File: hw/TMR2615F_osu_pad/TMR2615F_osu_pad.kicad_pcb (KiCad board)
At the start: 4 copper layers, 60 x 60 mm, 120 parts, among them J1 TYPE-C-31-M-12, J10 Conn_01x04, J2 TYPE-C-31-M-12, J3 Conn_01x02, J4 TYPE-C-31-M-12, J5 XY-SH1_0-4A61, J7 Conn_01x10, J8 Conn_01x06, J9 Conn_01x23, SW1 SKSGPAE010, SW2 SKSGPAE010, U1 CA-IS3722CHS, U10 TMR2615x, U11 CPG151101S11-16, U12 SK6812MINI-E, U13 TMR2615x, U14 CPG151101S11-16, U15 SK6812MINI-E, U16 TMR2615x, U17 CPG151101S11-16, U18 SK6812MINI-E, U19 TMR2615x, U2 SRV05-4A, U20 CPG151101S11-16, U21 SK6812MINI-E, U22 TMR2615x, U23 CPG151101S11-16, U24 SK6812MINI-E, U25 TMR2615x, U26 CPG151101S11-16, U27 SK6812MINI-E, U28 SRV05-4A, U3 TMUX1574RSVR, U4 LM66100DCK, U5 AP22653W6-7, U6 SRV05-4A, U7 AT32F405RBT7-7, U8 XC6206P332MR, U9 TPS7A4700, X1 X322512MSB4SI

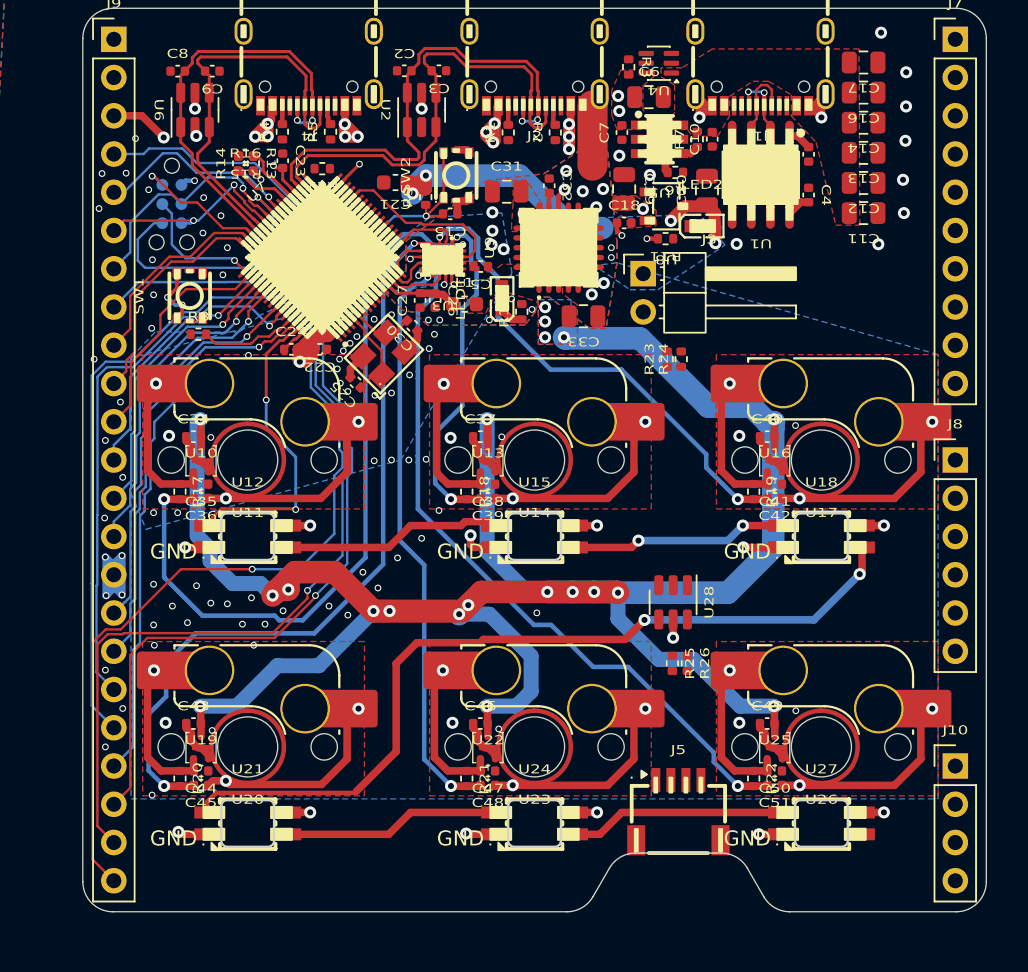
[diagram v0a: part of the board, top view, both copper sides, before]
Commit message: Update TMR2615F_osu_pad layout/schematic, bump library submodule, add ERC report
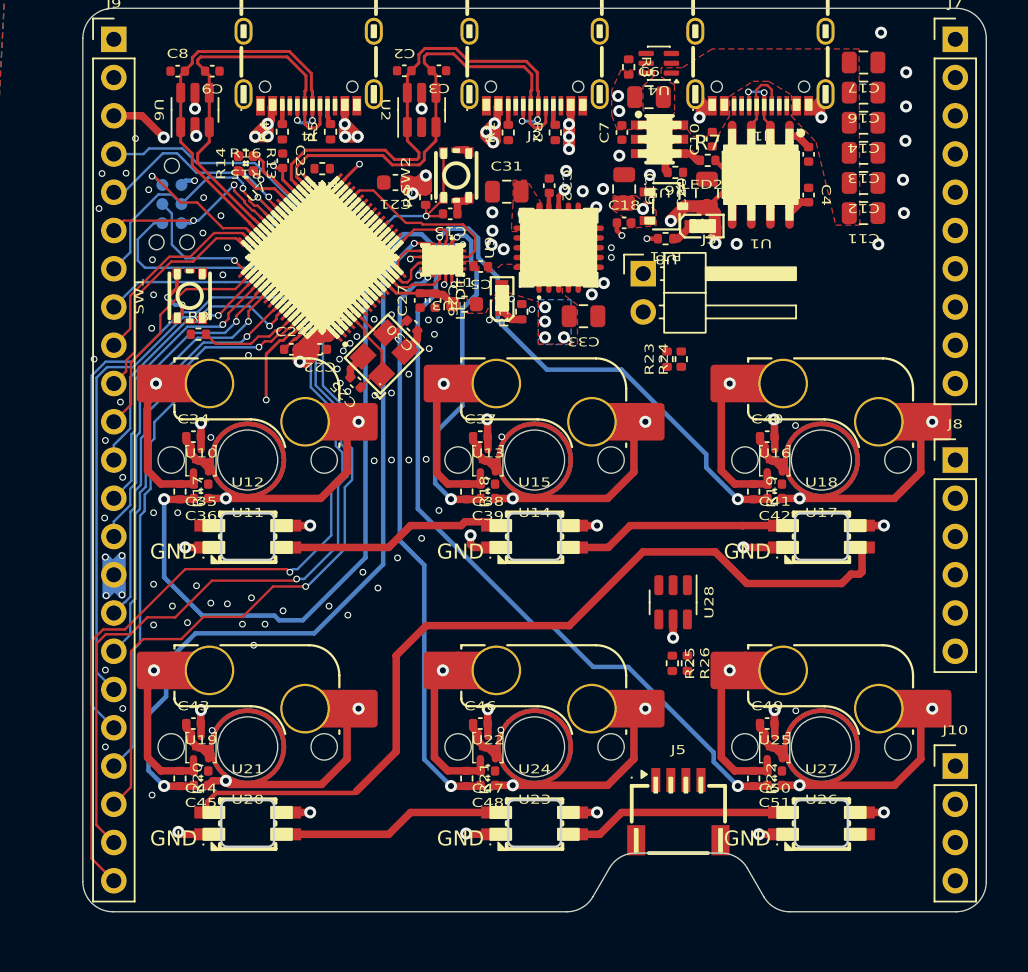
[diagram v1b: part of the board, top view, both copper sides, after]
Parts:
- removed NT1: NetTie_2, NetTie:NetTie-2_SMD_Pad2.0mm
- moved R7 1.57 mm to (124.6, 101.0), turned to 0 degrees
- moved C20 0.20 mm to (124.5, 103.2)
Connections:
- C26 pad 2: GNDA -> GND
- C27 pad 1: GNDA -> GND
- C31 pad 1: GNDA -> GND
- C32 pad 1: GNDA -> GND
- C33 pad 1: GNDA -> GND
- C34 pad 1: GNDA -> GND
- C35 pad 1: GNDA -> GND
- C36 pad 1: GNDA -> GND
- C37 pad 1: GNDA -> GND
- C38 pad 1: GNDA -> GND
- C39 pad 1: GNDA -> GND
- C40 pad 1: GNDA -> GND
- C41 pad 1: GNDA -> GND
- C42 pad 1: GNDA -> GND
- C43 pad 1: GNDA -> GND
- C44 pad 1: GNDA -> GND
- C45 pad 1: GNDA -> GND
- C46 pad 1: GNDA -> GND
- C47 pad 1: GNDA -> GND
- C48 pad 1: GNDA -> GND
- C49 pad 1: GNDA -> GND
- C5 pad 1: GNDA -> GND
- C50 pad 1: GNDA -> GND
- C51 pad 1: GNDA -> GND
- J8 pad 1: GNDA -> GND
- J9 pad 10: /I2C2_SDA -> /I2C2_SCL
- J9 pad 9: /I2C2_SCL -> /I2C2_SDA
- R10 pad 2: GNDA -> GND
- R7 pad 1: Net-(U5-FAULT#) -> /IO9
- R7 pad 2: /VBUS_B -> +3.3V
- U10 pad 2: GNDA -> GND
- U10 pad 4: GNDA -> GND
- U11 pad 1: GNDA -> GND
- U13 pad 2: GNDA -> GND
- U13 pad 4: GNDA -> GND
- U14 pad 1: GNDA -> GND
- U16 pad 2: GNDA -> GND
- U16 pad 4: GNDA -> GND
- U17 pad 1: GNDA -> GND
- U19 pad 2: GNDA -> GND
- U19 pad 4: GNDA -> GND
- U20 pad 1: GNDA -> GND
- U22 pad 2: GNDA -> GND
- U22 pad 4: GNDA -> GND
- U23 pad 1: GNDA -> GND
- U25 pad 2: GNDA -> GND
- U25 pad 4: GNDA -> GND
- U26 pad 1: GNDA -> GND
- U3 pad 6: GNDA -> GND
- U5 pad 3: /IO9 -> +5V
- U5 pad 4: Net-(U5-FAULT#) -> /IO9
- U7 pad 12: GNDA -> GND
- U9 pad 11: GNDA -> GND
- U9 pad 12: GNDA -> GND
- U9 pad 17: GNDA -> GND
- U9 pad 18: GNDA -> GND
- U9 pad 19: GNDA -> GND
- U9 pad 2: GNDA -> GND
- U9 pad 21: GNDA -> GND
- U9 pad 7: GNDA -> GND
- U9 pad 8: GNDA -> GND
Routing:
- net +5V: track 224.2 -> 29.5 mm
- net GND: track 44.7 -> 167.0 mm, vias 73 -> 134
- net GNDA: track 122.2 -> 0.00 mm, vias 69 -> 0
- net +3.3V: track 78.3 -> 30.9 mm
- net /DIN: track 20.8 -> 6.21 mm, vias 2 -> 1
- net +3.3VA: track 157.8 -> 147.0 mm, vias 20 -> 10
- net /Key2/DOUT: track 55.6 -> 57.6 mm, vias 2 -> 0
- net /IO9: track 0.00 -> 1.53 mm
- net Net-(LED2-K): track 0.00 -> 1.49 mm
- net Net-(U5-FAULT#): track 1.33 -> 0.00 mm
- net /IO7: track 52.1 -> 51.3 mm
- net /IO6: track 46.0 -> 45.3 mm
- net /Key1/DOUT: vias 2 -> 0
- removed copper zone on B.Cu, net +3.3V
- removed copper zone on In2.Cu, net +5V
- removed copper zone on B.Cu, net GNDA
- removed copper zone on F.Cu, net GNDA
- removed copper zone on In1.Cu, net GNDA
- removed copper zone on In2.Cu, net GNDA

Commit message: before foob
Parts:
- removed the C11 at (134.9, 104.6)
- removed the C13 at (134.9, 100.5)
- removed the C14 at (134.9, 98.5)
- removed the C16 at (134.9, 96.6)
- removed the C17 at (134.9, 94.5)
- removed the C35 at (91.0, 122.5)
- removed the C39 at (110.0, 123.5)
- removed the C47 at (110.0, 141.6)
- removed the C51 at (129.1, 142.6)
- removed the J3 at (120.3, 108.6)
- removed the R15 at (93.9, 100.8)
- removed the R16 at (93.9, 101.7)
- removed the R17 at (89.5, 123.0)
- removed the R18 at (108.6, 123.0)
- removed the R19 at (127.7, 123.0)
- removed the R20 at (89.5, 142.1)
- removed the R21 at (108.6, 142.1)
- removed the R22 at (127.7, 142.1)
- added C10, C34, C46, C54: CL10B473KB8NNNC, Capacitor_SMD:C_0603_1608Metric, F.Cu at (0.00, 0.00)
- added C2, C3, C6: CL21A226MAQNNNE, Capacitor_SMD:C_0805_2012Metric, F.Cu at (0.00, 0.00)
- added C28, C29, C40, C52, C56: CL05B104KB54PNC, Capacitor_SMD:C_0402_1005Metric, F.Cu at (0.00, 0.00)
- added C33, C37, C49, C53: 0402CG300J500NT, Capacitor_SMD:C_0402_1005Metric, F.Cu at (0.00, 0.00)
- added D1: 1N4148WS_T4, Diode_SMD:D_SOD-323_HandSoldering, F.Cu at (0.00, 0.00)
- added FID1, FID2, FID3: Fiducial, Fiducial:Fiducial_1mm_Mask2mm, F.Cu at (0.00, 0.00)
- added H1, H2, H3: MountingHole_Pad, MountingHole:MountingHole_2.2mm_M2_Pad_Via, F.Cu at (0.00, 0.00)
- added R1, R10, R2, R26, R4, R6, R9: 0402WGF1002TCE, Resistor_SMD:R_0402_1005Metric, F.Cu at (0.00, 0.00)
- added R12: 0402WGF5101TCE, Resistor_SMD:R_0402_1005Metric, F.Cu at (0.00, 0.00)
- added R27, R3: 0402WGF1200TCE, Resistor_SMD:R_0402_1005Metric, F.Cu at (0.00, 0.00)
- added R29, R30, R31, R32, R33, R34: 0402WGF3300TCE, Resistor_SMD:R_0402_1005Metric, F.Cu at (0.00, 0.00)
- added TP1, TP10, TP11, TP12, TP13, TP14, TP15, TP16, TP17, TP18, TP19, TP2, TP20, TP21, TP22, TP3, TP4, TP5, TP6, TP7, TP8, TP9: TestPoint, TestPoint:TestPoint_Pad_D1.0mm, B.Cu at (0.00, 0.00)
- added U12: SK6812MINI-E, LED__C:LED-SMD_4P-L3.2-W2.8-LS5.9_SK6812MINI-E, F.Cu at (0.00, 0.00)
- added U7: LM66100DCK, Package_TO_SOT_SMD:SOT-363_SC-70-6, F.Cu at (0.00, 0.00)
- C1, C4, C5: value CL05B104KB54PNC -> CL21A226MAQNNNE; footprint Capacitor_SMD:C_0402_1005Metric -> Capacitor_SMD:C_0805_2012Metric
- C12: value CL21A226MAQNNNE -> CL21A106KAYNNNE
- C36, C48: value 0402CG300J500NT -> CL05B104KB54PNC
- C38, C50: value CL05B104KB54PNC -> CL10B473KB8NNNC; footprint Capacitor_SMD:C_0402_1005Metric -> Capacitor_SMD:C_0603_1608Metric
- C41: value CL05B104KB54PNC -> 0402CG300J500NT
- C42: value 0402CG300J500NT -> CL10B473KB8NNNC; footprint Capacitor_SMD:C_0402_1005Metric -> Capacitor_SMD:C_0603_1608Metric
- R13: value 0402WGF0000TCE -> 0402WGF5101TCE
- R14: value 0402WGF0000TCE -> 0402WGF1200TCE
- R7: value 0402WGF1002TCE -> 0402WGF1200TCE
- R8: value 0402WGF3301TCE -> 0402WGF3300TCE
- U1: value CA-IS3722CHS -> SRV05-4A; footprint Isolator__C:SOIC-8_L4.9-W3.9-P1.27-LS6.0-BL -> Diode__C:SOT-23-6
- moved J8 199.6 mm to (0.00, 0.00)
- moved U24 196.2 mm to (0.00, 0.00)
- moved SW8 192.5 mm to (0.00, 0.00)
- moved C50 191.6 mm to (0.00, 0.00), turned to 0 degrees
- moved U23 190.4 mm to (0.00, 0.00)
- moved J4 189.3 mm to (0.00, 0.00)
- moved C55 188.9 mm to (0.00, 0.00)
- moved J7 185.8 mm to (0.00, 0.00)
- moved U22 184.0 mm to (0.00, 0.00)
- moved U18 182.6 mm to (0.00, 0.00)
- moved R16 182.4 mm to (0.00, 0.00), turned to 0 degrees
- moved R21 181.7 mm to (0.00, 0.00), turned to 0 degrees
- moved C48 180.1 mm to (0.00, 0.00), turned to 0 degrees
- moved SW7 180.0 mm to (0.00, 0.00)
- moved SW5 179.1 mm to (0.00, 0.00)
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- renumbered C10 to C11, C31 to C13, C32 to C14, C8 to C15, C9 to C16, C2 to C17, C3 to C18, C18 to C19, C19 to C20, C20 to C21, C26 to C22, C27 to C23, C21 to C24, C22 to C25, C23 to C26, C24 to C27, C15 to C30, C25 to C31, C30 to C32, C34 to C35, C37 to C39, C40 to C43, C43 to C47, C46 to C51, C49 to C55, C6 to C7, C7 to C8, C33 to C9, J4 to J2, J2 to J3, J5 to J4, J7 to J5, J9 to J6, J8 to J7, J10 to J8, J6 to J9, R6 to R11, R24 to R15, R26 to R16, R4 to R17, R5 to R18, R1 to R19, R2 to R20, R25 to R21, R23 to R22, R10 to R23, R11 to R24, R12 to R25, R9 to R28, R3 to R5, U11 to SW3, U14 to SW4, U17 to SW5, U20 to SW6, U23 to SW7, U26 to SW8, U7 to U10, U3 to U11, U10 to U13, U12 to U14, U13 to U15, U15 to U16, U16 to U17, U4 to U2, U21 to U20, U22 to U21, U24 to U22, U25 to U23, U27 to U24, U5 to U3, U9 to U4, U6 to U5, U2 to U6, U28 to U9
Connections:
- net /IO10 renamed /LM_ST
- C1 pad 2: Net-(U1-VDDA) -> +5V
- C11 pad 2: /VBUS_B -> VBUS_B
- C12 pad 1: GND -> VBUS_B
- C12 pad 2: /VBUS_B -> GND
- C36 pad 2: /TMUX_S1A -> +5V
- C38 pad 2: Net-(U13-VOUT) (its old number) -> /TMUX_S1B
- C4 pad 2: Net-(U1-VDDB) -> +5V
- C44 pad 2: Net-(U19-VOUT) -> +5V
- C45 pad 2: /TMUX_S2B -> Net-(U19-VOUT)
- C48 pad 2: /TMUX_S3A -> +5V
- C5 pad 2: +3.3VA -> +5V
- C50 pad 2: Net-(U25-VOUT) -> /TMUX_S3A
- C7 pad 1: +5V -> VBUS_HOST
- C8 pad 2: +5V -> VBUS_HOST
- J1 pad A4B9: /VBUS_B -> VBUS_B
- J1 pad A5: unconnected-(J1-CC1-PadA5) -> Net-(J1-CC1)
- J1 pad B4A9: /VBUS_B -> VBUS_B
- J1 pad B5: unconnected-(J1-CC2-PadB5) -> Net-(J1-CC2)
- J2 pad A4B9: +5V -> unconnected-(J2-VBUS-PadA4B9)
- J2 pad B4A9: +5V -> unconnected-(J2-VBUS-PadB4A9)
- J3 pad A4B9: +5V -> VBUS_HOST
- J3 pad B4A9: +5V -> VBUS_HOST
- J5 pad 10: /TMUX_S4A -> /TMUX_S4B
- J5 pad 9: /TMUX_S4B -> GND
- J6 pad 10: /I2C2_SCL -> /I2C2_SDA
- J6 pad 11: /SPI3_CS -> /I2C2_SCL
- J6 pad 12: /SPI3_SCK -> /SPI3_CS
- J6 pad 13: /SPI3_MISO -> /SPI3_SCK
- J6 pad 14: /SPI3_MOSI -> /SPI3_MISO
- J6 pad 15: GND -> /SPI3_MOSI
- J6 pad 16: /IO1 -> GND
- J6 pad 17: /IO2 -> /IO1
- J6 pad 18: /IO3 -> /IO2
- J6 pad 19: /IO4 -> /IO3
- J6 pad 2: +5V -> GND
- J6 pad 20: /IO5 -> /IO4
- J6 pad 21: /IO6 -> /IO5
- J6 pad 22: /IO7 -> /IO6
- J6 pad 23: /IO8 -> /IO7
- J6 pad 3: +3.3V -> +5V
- J6 pad 4: /UART8_TX -> +3.3V
- J6 pad 5: /UART8_RX -> /UART8_TX
- J6 pad 6: /USART1_RX -> /UART8_RX
- J6 pad 7: /USART1_TX -> /USART1_RX
- J6 pad 8: /USART1_CK -> /USART1_TX
- J6 pad 9: /I2C2_SDA -> /USART1_CK
- R13 pad 1: Net-(U7-PC6) -> GND
- R13 pad 2: /UART7_TX -> Net-(J1-CC1)
- R14 pad 1: Net-(U7-PC7) -> Net-(R14-Pad1)
- R14 pad 2: /UART7_RX -> +3.3V
- R15 pad 2: Net-(J3-Pin_2) -> Net-(R14-Pad1)
- R22 pad 2: Net-(J3-Pin_2) -> Net-(R14-Pad1)
- R5 pad 2: +5V -> +3.3V
- R7 pad 1: /IO9 -> Net-(J1-DP1)
- R7 pad 2: +3.3V -> /UART7_TX
- R8 pad 1: GND -> /TMUX_S4A
- R8 pad 2: /BOOT -> Net-(C10-Pad2)
- SW4 pad 2: Net-(U13-VOUT) (its old number) -> Net-(U15-VOUT)
- SW8 pad 2: Net-(U25-VOUT) -> Net-(U23-VOUT)
- U1 pad 1: Net-(U1-VDDA) -> /UART7_RX
- U1 pad 2: Net-(J1-DP1) -> GND
- U1 pad 3: Net-(J1-DN1) -> /UART7_TX
- U1 pad 4: GND -> /UART7_TX
- U1 pad 5: GND -> +3.3V
- U10 pad 2: /IO6 -> /PW_PSTRH
- U10 pad 29: /IO9 -> /AP_FAULT
- U10 pad 3: /IO7 -> /IO6
- U10 pad 37: Net-(U7-PC6) -> /UART7_RX
- U10 pad 38: Net-(U7-PC7) -> /UART7_TX
- U10 pad 4: /IO8 -> /IO7
- U10 pad 62: /DIN -> Net-(U10-PB9)
- U11 pad 13: +3.3VA -> GND
- U15 pad 1: Net-(U13-VOUT) (its old number) -> Net-(U15-VOUT)
- U2 pad 1: /VBUS_B -> VBUS_B
- U2 pad 3: GND -> +5V
- U23 pad 1: Net-(U25-VOUT) -> Net-(U23-VOUT)
- U3 pad 1: +5V -> VBUS_HOST
- U3 pad 3: +5V -> /PW_PSTRH
- U3 pad 4: /IO9 -> /AP_FAULT
- U3 pad 6: /VBUS_B -> VBUS_B
- U9 pad 1: /I2C1_SCL -> /I2C1_SDA
- U9 pad 3: /I2C1_SDA -> /I2C1_SCL
- U9 pad 4: /I2C1_SDA -> /I2C1_SCL
- U9 pad 5: +5V -> +3.3V
- U9 pad 6: /I2C1_SCL -> /I2C1_SDA
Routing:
- net +5V: track 29.5 -> 254.4 mm, vias 26 -> 19
- net +3.3V: track 30.9 -> 176.1 mm, vias 9 -> 17
- net GND: track 167.0 -> 30.9 mm, vias 134 -> 473
- net /I2C3_SCL: track 0.00 -> 68.5 mm, vias 0 -> 1
- net /IO8: track 54.9 -> 0.00 mm, vias 2 -> 0
- net /I2C3_SDA: track 0.00 -> 52.7 mm, vias 0 -> 2
- net Net-(U10-PB9): track 0.00 -> 49.6 mm, vias 0 -> 2
- net /I2C1_SDA: track 0.00 -> 43.5 mm, vias 0 -> 2
- net /ADC1_IN11: track 0.00 -> 42.8 mm, vias 0 -> 2
- net /ADC1_IN10: track 0.00 -> 42.3 mm, vias 0 -> 2
- net /I2C1_SCL: track 0.00 -> 41.7 mm, vias 0 -> 2
- net /ADC1_IN12: track 0.00 -> 40.4 mm, vias 0 -> 2
- net /ADC1_IN5: track 0.00 -> 39.2 mm, vias 0 -> 1
- net /ADC1_IN13: track 0.00 -> 38.2 mm, vias 0 -> 2
- net /UART7_TX: track 0.77 -> 32.8 mm, vias 1 -> 2
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- added copper zone on B.Cu, net +3.3V
- added copper zone on F.Cu, net +3.3V
- added copper zone on In2.Cu, net +3.3V
- added copper zone on In2.Cu, net +5V
- added copper zone on F.Cu, net Net-(C10-Pad2)
- added copper zone on F.Cu, net VBUS_B
- added copper zone on In2.Cu, net VBUS_B
- added copper zone on F.Cu, net VBUS_HOST
- removed copper zone on In1.Cu, net +3.3VA
- removed copper zone on F.Cu, net /VBUS_B
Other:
- board size 60 x 60 mm -> 70.1 x 60 mm
